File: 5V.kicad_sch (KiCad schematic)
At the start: 5 parts, among them U4 PINA740BIREMR

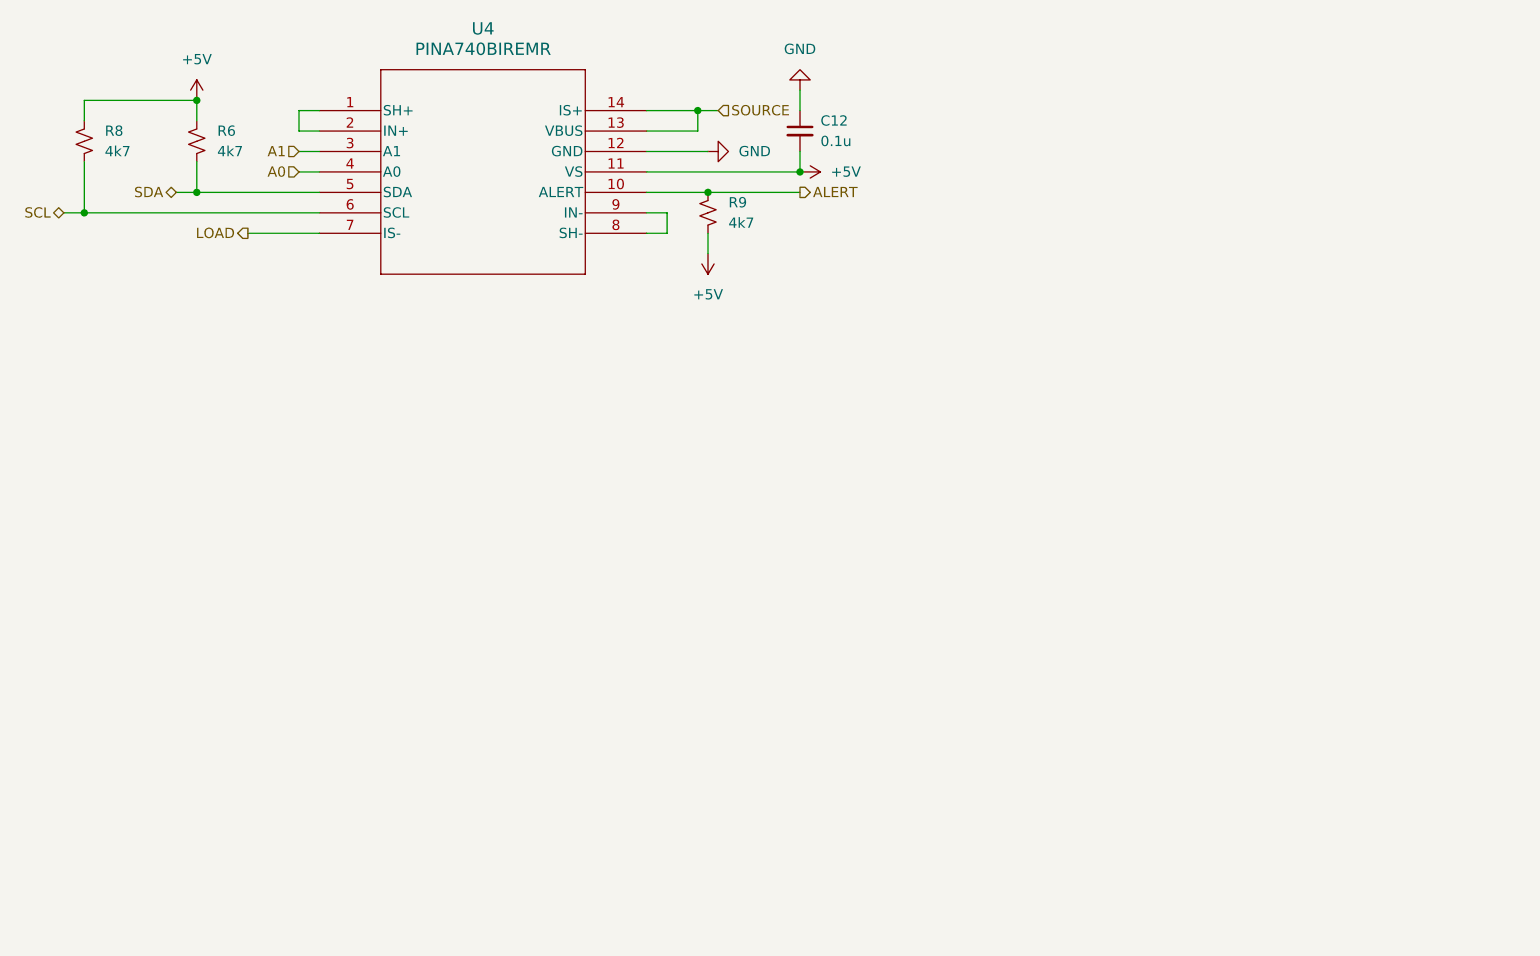
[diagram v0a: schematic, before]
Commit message: Buck-boost 5V entry
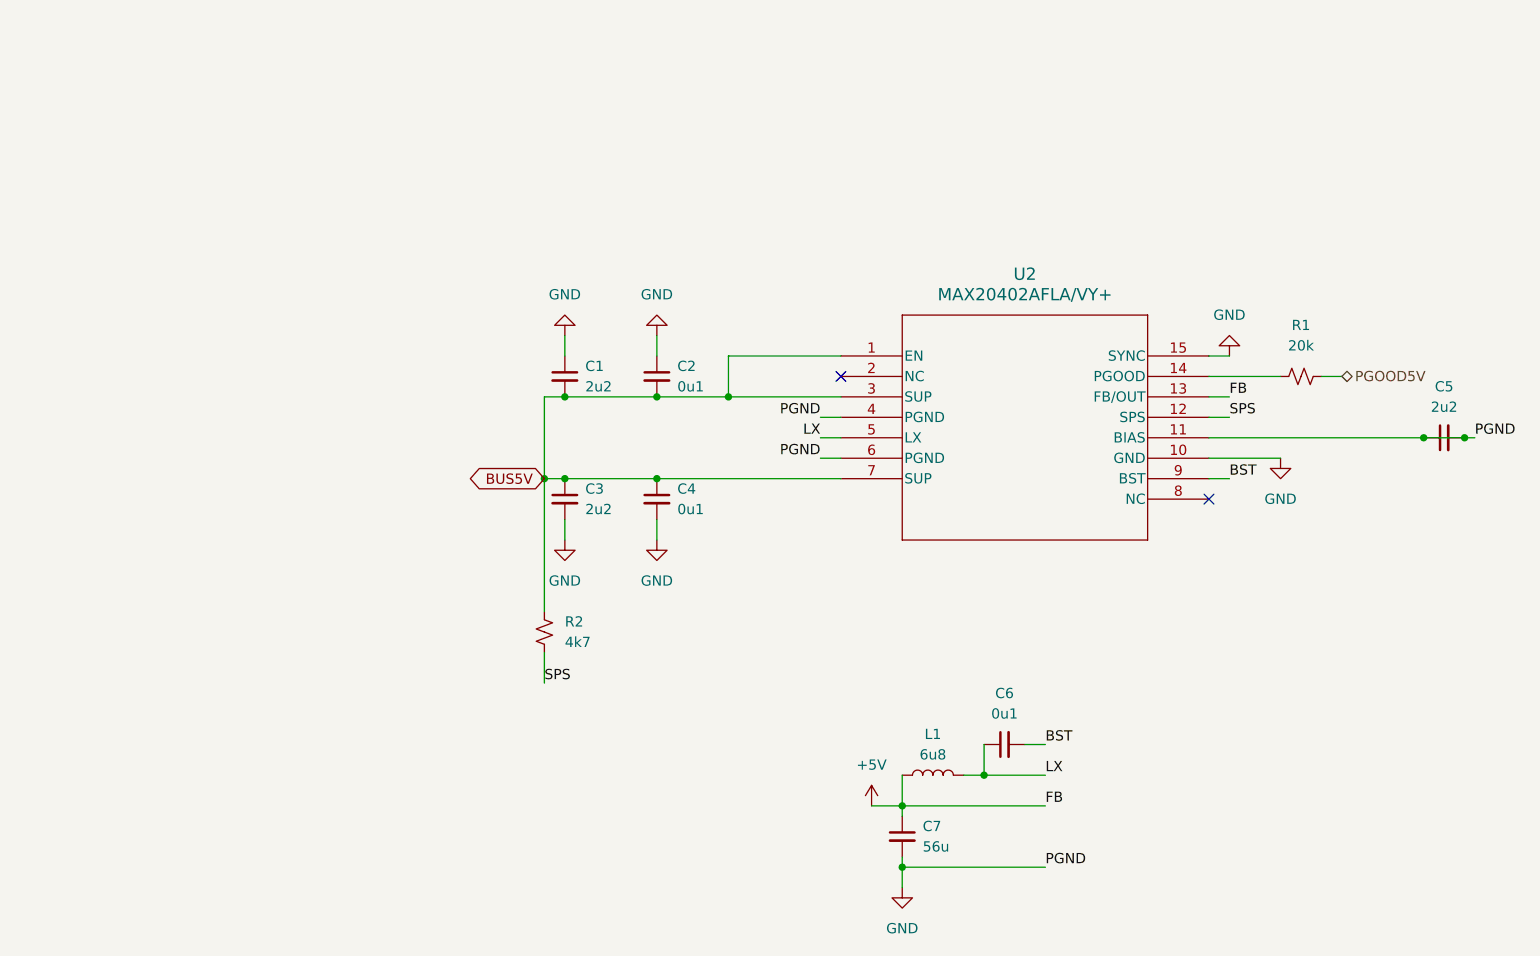
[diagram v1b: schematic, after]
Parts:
- removed C12: 0.1u, symbol Device:C_Small
- removed R6, R8, R9: 4k7, symbol Device:R_Small_US
- removed U4: PINA740BIREMR, VQFN14_REM_TEX, symbol INA740B:PINA740BIREMR
- added C1, C3, C5: 2u2, symbol Device:C_Small
- added C2, C4, C6: 0u1, symbol Device:C_Small
- added C7: 56u, symbol Device:C_Small
- added L1: 6u8, symbol Device:L
- added R1: 20k, symbol Device:R_Small_US
- added R2: 4k7, symbol Device:R_Small_US
- added U2: MAX20402AFLA/VY+, 21-100532_90-100188_ADI, symbol MAX20402A:MAX20402AFLA_VY+
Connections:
- net +5V: now also C7.1, L1.1, U2.13 (FB/OUT)
- net GND: now also C1.1, C2.1, C3.2, C4.2, C5.1, C5.2, C7.2, U2.10 (GND), U2.11 (BIAS), U2.15 (SYNC), U2.4 (PGND), U2.6 (PGND)
- new net: R1.1, U2.14 (PGOOD)
- new net BST: C6.2, U2.9 (BST)
- new net BUS5V: C1.2, C2.2, C3.1, C4.1, R2.2, U2.1 (EN), U2.3 (SUP), U2.7 (SUP)
- new net LX: C6.1, L1.2, U2.5 (LX)
- new net PGOOD5V: R1.2
- new net SPS: R2.1, U2.12 (SPS)
- no-connect marks 0 -> 2
